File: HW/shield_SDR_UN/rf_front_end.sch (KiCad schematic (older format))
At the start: 93 parts, among them Q1 MOSFET_P, U1 MAX5864, U2 MAX2830

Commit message: Schematic finished
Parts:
- removed C?: 0, symbol Device:C
- removed FB?: FILTER, symbol hackrf-one-packages:FILTER
- removed P?: GSG-RF-CONN, symbol hackrf-one-rescue:GSG-RF-CONN
- removed R7, R? (x2): 4.7k, Resistor_SMD:R_0603_1608Metric_Pad1.05x0.95mm_HandSolder, symbol Device:R
- removed R? (x3): 0, symbol Device:R
- removed T?: BALUN, symbol hackrf-one-rescue:BALUN
- added C39: 0, Capacitor_SMD:C_0603_1608Metric_Pad1.05x0.95mm_HandSolder, symbol Device:C
- added P2: GSG-RF-CONN, lib:TAOGLAS_EMPCB.SMAFSTJ.B.HT, symbol hackrf-one-rescue:GSG-RF-CONN
- added R10, R11, R9: 0, Resistor_SMD:R_0603_1608Metric_Pad1.05x0.95mm_HandSolder, symbol Device:R
- added R13, R14, R15: 4.7k, Resistor_SMD:R_0603_1608Metric_Pad1.05x0.95mm_HandSolder, symbol Device:R
- added T1: BALUN, lib:HHM1711E1, symbol hackrf-one-rescue:BALUN
- C40: renamed from C?; footprint (none) -> Capacitor_SMD:C_0603_1608Metric_Pad1.05x0.95mm_HandSolder; Digikey RMCF0402ZT0R00CT-ND -> RMCF0603ZT0R00CT-ND
- FB1: footprint (none) -> Inductor_SMD:L_0805_2012Metric_Pad1.15x1.40mm_HandSolder; Digikey (none) -> BLM21PG221SN1D
- P1: renamed from P?; footprint (none) -> lib:TAOGLAS_EMPCB.SMAFSTJ.B.HT; Digikey (none) -> CON-SMA-EDGE-S-ND
- Q1: footprint (none) -> DMP2305U-7:SOT103P240X110-3N; Digikey (none) -> DMP2305UDICT-ND
- R12: renamed from R?; footprint (none) -> Resistor_SMD:R_0603_1608Metric_Pad1.05x0.95mm_HandSolder; Digikey RMCF0402ZT0R00CT-ND -> RMCF0603ZT0R00CT-ND
- R16: renamed from R?; DESCRIPTION 4.7 kOhms ±1% 0.1W, 1/10W -> (none); DIGIKEY 311-4.70KHRCT-ND -> (none); Digikey (none) -> 311-4.70KHRCT-ND
- T2: renamed from T?; footprint (none) -> lib:HHM1711E1; Digikey (none) -> 445-172632-1-ND
- gave numbers to parts that had none: 69
- renumbered C5 to C10, C2 to C5, C3 to C6, R6 to R20, U2 to U1, U1 to U3
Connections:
- net GNDA is gone; now on net GND: C11.2, C12.2, C13.2, C14.2, C15.2, C16.2, C17.2, C18.2, C19.2, C2.2, C20.2, C21.2, C22.2, C23.2, C24.2, C25.2, C26.2, C27.2, C28.2, C29.2, C3.2, C30.2, C31.2, C32.2, C33.2, C34.2, C35.2, C36.2, C37.2, C38.2, C4.2, C41.2, C42.2, C44.1, C45.1, C47.1, C48.1, C5.2, C7.2, C8.2, C9.2, CA1.2, D1.1 (K), P1.2 (GND), R16.1, T2.2 (S2), T2.5 (PM), U1.0 (EP), U1.2 (GNDRXLNA), U1.26 (GNDCP), U1.31 (GNDVCO), U3.0 (EP), U3.12 (GND), U3.37 (GND), U3.42 (GND), U3.5 (GND), U3.7 (GND)
- net GND: now also P2.2 (GND), R13.1, R14.1, R15.1, T1.2 (S2), T1.5 (PM)
- net IA+: now also R9.2
- net IA-: now also R10.2
- net QA-: now also R11.2
- net RXBBI+: now also R9.1
- net RXBBI-: now also R10.1
- net RXBBQ+: now also R11.1
- net TXBBI+: now also R13.2
- net TXBBI-: now also R14.2
- net TXBBQ+: now also R15.2
- net at U1.4 (ANT1+): now also T1.4 (PR2)
- net at U1.5 (ANT1-): now also T1.3 (PR1)
- net at U1.9 (ANT2+): now also C39.1
- net at P1.1 (RF): now also T1.1 (S1)
- net at T2.1 (S1): now also P2.1 (RF)
- net at T2.4 (PR2): now also C39.2
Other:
- note removed: "OJO CON ESTOS PINES LOS COLOQUE \nCOMO EL HACK COMUNICACION CON EL MICRO"

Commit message: organizacion PCB
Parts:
- Q1: footprint DMP2305U-7:SOT103P240X110-3N -> lib:SOT103P240X110-3N
- U1: footprint FP-MAX2830:MAX2830ETM&plus_ -> lib:MAX2830ETM&plus_
- U2: footprint QFN50P300X300X60-21N:QFN50P300X300X60-21N -> lib:QFN50P300X300X60-21N
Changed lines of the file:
@@
 Text Label 11800 3650 0    50   ~ 0
 REFP
-Text Label 14350 4050 0    50   ~ 0
+Text Label 14600 4050 2    50   ~ 0
 adDD9
-Text Label 14350 4150 0    50   ~ 0
+Text Label 14600 4150 2    50   ~ 0
 adDD8
-Text Label 14350 4250 0    50   ~ 0
+Text Label 14600 4250 2    50   ~ 0
 adDD7
-Text Label 14350 4350 0    50   ~ 0
+Text Label 14600 4350 2    50   ~ 0
 adDD6
-Text Label 14350 4450 0    50   ~ 0
+Text Label 14600 4450 2    50   ~ 0
 adDD5
-Text Label 14350 4550 0    50   ~ 0
+Text Label 14600 4550 2    50   ~ 0
 adDD4
-Text Label 14350 4650 0    50   ~ 0
+Text Label 14600 4650 2    50   ~ 0
 adDD3
-Text Label 14350 4750 0    50   ~ 0
+Text Label 14600 4750 2    50   ~ 0
 adDD2
 Text Label 13700 5650 1    50   ~ 0
@@
 QA+
 Wire Wire Line
-	13600 5400 13600 5800
-Wire Wire Line
 	13700 5400 13700 5800
-Wire Wire Line
-	14350 4050 14700 4050
-Wire Wire Line
-	14350 4150 14700 4150
-Wire Wire Line
-	14350 4250 14700 4250
-Wire Wire Line
-	14350 4350 14700 4350
-Wire Wire Line
-	14350 4450 14700 4450
-Wire Wire Line
-	14350 4550 14700 4550
-Wire Wire Line
-	14350 4650 14700 4650
-Wire Wire Line
-	14350 4750 14700 4750
-Text GLabel 14700 4050 2    50   Input ~ 0
+Text GLabel 14800 4050 2    50   Input ~ 0
 adDD9
-Text GLabel 14700 4150 2    50   Input ~ 0
+Text GLabel 14800 4150 2    50   Input ~ 0
 adDD8
-Text GLabel 14700 4250 2    50   Input ~ 0
+Text GLabel 14800 4250 2    50   Input ~ 0
 adDD7
-Text GLabel 14700 4350 2    50   Input ~ 0
+Text GLabel 14800 4350 2    50   Input ~ 0
 adDD6
-Text GLabel 14700 4450 2    50   Input ~ 0
+Text GLabel 14800 4450 2    50   Input ~ 0
 adDD5
-Text GLabel 14700 4550 2    50   Input ~ 0
+Text GLabel 14800 4550 2    50   Input ~ 0
 adDD4
-Text GLabel 14700 4650 2    50   Input ~ 0
+Text GLabel 14800 4650 2    50   Input ~ 0
 adDD3
-Text GLabel 14700 4750 2    50   Input ~ 0
+Text GLabel 14800 4750 2    50   Input ~ 0
 adDD2
 Text GLabel 13700 5800 3    50   Input ~ 0
@@
 adDA0
 Wire Wire Line
-	12800 2900 12800 3000
-Wire Wire Line
 	13100 2900 13100 3000
 Wire Wire Line
@@
 L power:VAA #PWR069
 U 1 1 5CCBDAAC
-P 14500 3950
-F 0 "#PWR069" H 14500 3800 50  0001 C CNN
-F 1 "VAA" V 14500 4150 50  0000 C CNN
-F 2 "" H 14500 3950 50  0001 C CNN
-F 3 "" H 14500 3950 50  0001 C CNN
-	1    14500 3950
+P 14550 3950
+F 0 "#PWR069" H 14550 3800 50  0001 C CNN
+F 1 "VAA" V 14550 4150 50  0000 C CNN
+F 2 "" H 14550 3950 50  0001 C CNN
+F 3 "" H 14550 3950 50  0001 C CNN
+	1    14550 3950
 	0    1    1    0
 $EndComp
-Wire Wire Line
-	14500 3950 14350 3950
 $Comp
 L power:VAA #PWR057
@@
 F 0 "Q1" H 1150 1250 60  0000 L CNN
 F 1 "MOSFET_P" H 800 1550 60  0000 L CNN
-F 2 "DMP2305U-7:SOT103P240X110-3N" H 1350 1400 60  0001 C CNN
+F 2 "lib:SOT103P240X110-3N" H 1350 1400 60  0001 C CNN
 F 3 "https://www.diodes.com/assets/Datasheets/ds31737.pdf" H 1350 1400 60  0001 C CNN
 F 4 "DMP2305UDICT-ND" H 1350 1400 50  0001 C CNN "Digikey"
@@
 	1250 3200 1250 3100
 $Comp
-L power:VCC #PWR064
-U 1 1 5CD923B4
-P 13100 5500
-F 0 "#PWR064" H 13100 5350 50  0001 C CNN
-F 1 "VCC" V 13100 5700 50  0000 C CNN
-F 2 "" H 13100 5500 50  0001 C CNN
-F 3 "" H 13100 5500 50  0001 C CNN
-	1    13100 5500
-	-1   0    0    1
-$EndComp
-Wire Wire Line
-	13100 5500 13100 5400
-$Comp
 L Device:C C5
 U 1 1 5CD06356
@@
 L power:VAA #PWR02
 U 1 1 5CDED280
-P 1200 7450
-F 0 "#PWR02" H 1200 7300 50  0001 C CNN
-F 1 "VAA" H 1200 7600 50  0000 C CNN
-F 2 "" H 1200 7450 50  0001 C CNN
-F 3 "" H 1200 7450 50  0001 C CNN
-	1    1200 7450
+P 1200 7400
+F 0 "#PWR02" H 1200 7250 50  0001 C CNN
+F 1 "VAA" H 1200 7550 50  0000 C CNN
+F 2 "" H 1200 7400 50  0001 C CNN
+F 3 "" H 1200 7400 50  0001 C CNN
+	1    1200 7400
 	1    0    0    -1
 $EndComp
@@
 	1200 8200 1200 8150
 Wire Wire Line
-	1200 7450 1200 7550
-Wire Wire Line
 	1600 7700 1600 7550
 Wire Wire Line
 	1600 7550 1200 7550
-Connection ~ 1200 7550
 Wire Wire Line
 	1200 7550 1200 7700
@@
 F 0 "U1" H 7600 4350 60  0000 L CNN
 F 1 "MAX2830" H 7450 4250 60  0000 L CNN
-F 2 "FP-MAX2830:MAX2830ETM&plus_" H 7650 4300 60  0001 C CNN
+F 2 "lib:MAX2830ETM&plus_" H 7650 4300 60  0001 C CNN
 F 3 "https://datasheets.maximintegrated.com/en/ds/MAX2830.pdf" H 7650 4300 60  0001 C CNN
 F 4 "MAX2830ETM+TCT-ND" H 7650 4300 50  0001 C CNN "Digikey"
@@
 	9000 4750 8850 4750
 $Comp
-L power:VAA #PWR025
-U 1 1 5CDC13A5
-P 6300 3750
-F 0 "#PWR025" H 6300 3600 50  0001 C CNN
-F 1 "VAA" V 6300 3950 50  0000 C CNN
-F 2 "" H 6300 3750 50  0001 C CNN
-F 3 "" H 6300 3750 50  0001 C CNN
-	1    6300 3750
-	0    -1   -1   0
-$EndComp
-$Comp
 L power:VAA #PWR027
 U 1 1 5CDC41DC
@@
 	9000 4350 8850 4350
 Wire Wire Line
-	9000 4650 8850 4650
-Wire Wire Line
 	8850 4850 9000 4850
 Wire Wire Line
@@
 NoConn ~ 10650 8950
 NoConn ~ 10550 8950
-Text GLabel 10850 9250 3    50   Input ~ 0
-3V3 MCU
-Wire Wire Line
-	10850 9250 10850 8950
 Wire Wire Line
 	11250 9100 10750 9100
@@
 Text GLabel 11800 9100 2    50   Input ~ 0
 GPIO_CLK
-Text GLabel 11800 8350 2    50   Input ~ 0
-3V3 MCU
-Wire Wire Line
-	11800 8350 11450 8350
-Text GLabel 10450 6800 1    50   Input ~ 0
-3V3 MCU
 $Comp
 L power:GND #PWR046
@@
 Text Notes 11550 7900 0    50   ~ 0
 MCU GP_CLKIN
-Text GLabel 11550 8050 2    50   Input ~ 0
-3V3 MCU
 Wire Wire Line
 	11550 8050 11450 8050
-Text GLabel 10650 7200 1    50   Input ~ 0
-3V3 MCU
-Wire Wire Line
-	10650 7200 10650 7350
 NoConn ~ 10550 7350
 $Comp
@@
 	1    0    0    -1
 $EndComp
-Text GLabel 8850 7550 1    50   Input ~ 0
-3V3 MCU
-Text GLabel 8650 7550 1    50   Input ~ 0
-3V3 MCU
-Text GLabel 8450 7550 1    50   Input ~ 0
-3V3 MCU
 Wire Wire Line
 	8450 7550 8450 7750
@@
 L power:VAA #PWR06
 U 1 1 5CEC6014
-P 1200 10100
-F 0 "#PWR06" H 1200 9950 50  0001 C CNN
-F 1 "VAA" H 1200 10250 50  0000 C CNN
-F 2 "" H 1200 10100 50  0001 C CNN
-F 3 "" H 1200 10100 50  0001 C CNN
-	1    1200 10100
+P 1200 10050
+F 0 "#PWR06" H 1200 9900 50  0001 C CNN
+F 1 "VAA" H 1200 10200 50  0000 C CNN
+F 2 "" H 1200 10050 50  0001 C CNN
+F 3 "" H 1200 10050 50  0001 C CNN
+	1    1200 10050
 	1    0    0    -1
 $EndComp
@@
 	1200 10850 1200 10800
 Wire Wire Line
-	1200 10100 1200 10200
-Wire Wire Line
 	1600 10350 1600 10200
 Wire Wire Line
 	1600 10200 1200 10200
-Connection ~ 1200 10200
 Wire Wire Line
 	1200 10200 1200 10350
@@
 NoConn ~ 8850 3950
 Wire Wire Line
-	7200 3100 7200 2900
-Wire Wire Line
 	7100 3100 7100 2900
 Text GLabel 7200 2900 1    50   Input ~ 0
@@
 F 0 "U2" H 10600 8200 60  0000 L CNN
 F 1 "SI5351C" H 10450 8050 60  0000 L CNN
-F 2 "QFN50P300X300X60-21N:QFN50P300X300X60-21N" H 10650 8150 60  0001 C CNN
+F 2 "lib:QFN50P300X300X60-21N" H 10650 8150 60  0001 C CNN
 F 3 "https://www.silabs.com/documents/public/data-sheets/Si5351-B.pdf" H 10650 8150 60  0001 C CNN
 F 4 "336-5160-1-ND" H 10650 8150 50  0001 C CNN "Digikey"
@@
 	1    0    0    -1
 $EndComp
-Text GLabel 14000 6600 0    50   Input ~ 0
-3V3 MCU
 Wire Wire Line
 	13400 6850 13400 6800
@@
 	14000 6800 14300 6800
 Wire Wire Line
-	14000 6800 14000 6600
-Wire Wire Line
 	13700 6850 13700 6800
 Connection ~ 13700 6800
@@
 SPI1_SCK
 Wire Wire Line
-	6450 3750 6300 3750
-Wire Wire Line
 	1250 6700 1250 6600
 Connection ~ 1250 6600
 Wire Wire Line
 	2150 5450 2150 5350
+Wire Wire Line
+	9000 4650 8850 4650
+Wire Wire Line
+	12800 2900 12800 3000
+Wire Wire Line
+	11800 8350 11450 8350
+Wire Wire Line
+	7200 2900 7200 3100
+Wire Wire Line
+	14350 4550 14800 4550
+Wire Wire Line
+	14350 4450 14800 4450
+Wire Wire Line
+	14550 3950 14350 3950
+Wire Wire Line
+	1200 7400 1200 7550
+Connection ~ 1200 7550
+$Comp
+L power:VAA #PWR0155
+U 1 1 5CEEB354
+P 6200 3750
+F 0 "#PWR0155" H 6200 3600 50  0001 C CNN
+F 1 "VAA" V 6200 3950 50  0000 C CNN
+F 2 "" H 6200 3750 50  0001 C CNN
+F 3 "" H 6200 3750 50  0001 C CNN
+	1    6200 3750
+	0    -1   -1   0
+$EndComp
+Wire Wire Line
+	6200 3750 6450 3750
+Wire Wire Line
+	1200 10050 1200 10200
+Connection ~ 1200 10200
+$Comp
+L power:VCC #PWR0156
+U 1 1 5CF2950C
+P 13100 5800
+F 0 "#PWR0156" H 13100 5650 50  0001 C CNN
+F 1 "VCC" V 13100 6000 50  0000 C CNN
+F 2 "" H 13100 5800 50  0001 C CNN
+F 3 "" H 13100 5800 50  0001 C CNN
+	1    13100 5800
+	-1   0    0    1
+$EndComp
+Wire Wire Line
+	13100 5400 13100 5800
+Wire Wire Line
+	13600 5400 13600 5800
+Wire Wire Line
+	14350 4650 14800 4650
+Wire Wire Line
+	14350 4350 14800 4350
+Wire Wire Line
+	14350 4250 14800 4250
+Wire Wire Line
+	14350 4150 14800 4150
+Wire Wire Line
+	14350 4050 14800 4050
+Wire Wire Line
+	14350 4750 14800 4750
+Wire Wire Line
+	10650 7350 10650 6800
+Wire Wire Line
+	14000 6800 14000 6600
+Wire Wire Line
+	14000 6600 13850 6600
+Text GLabel 10850 9350 3    50   Input ~ 0
+3V3 MCU
+Wire Wire Line
+	10850 8950 10850 9350
+Text GLabel 11800 8350 2    50   Input ~ 0
+3V3 MCU
+Text GLabel 11550 8050 2    50   Input ~ 0
+3V3 MCU
+Text GLabel 10450 6800 1    50   Input ~ 0
+3V3 MCU
+Text GLabel 10650 6800 1    50   Input ~ 0
+3V3 MCU
+Text GLabel 8450 7550 1    50   Input ~ 0
+3V3 MCU
+Text GLabel 8650 7550 1    50   Input ~ 0
+3V3 MCU
+Text GLabel 8850 7550 1    50   Input ~ 0
+3V3 MCU
+Text GLabel 13850 6600 0    50   Input ~ 0
+3V3 MCU
 $EndSCHEMATC

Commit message: Omega 2 PCB
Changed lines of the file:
@@
 Text Label 11800 3650 0    50   ~ 0
 REFP
-Text Label 14600 4050 2    50   ~ 0
+Text Label 14675 4050 2    50   ~ 0
 adDD9
 Text Label 14600 4150 2    50   ~ 0
@@
 $EndComp
 Wire Wire Line
-	7300 2950 7300 3100
-Wire Wire Line
 	7800 2950 7800 3100
 Wire Wire Line
@@
 	14350 4150 14800 4150
 Wire Wire Line
-	14350 4050 14800 4050
-Wire Wire Line
 	14350 4750 14800 4750
 Wire Wire Line
@@
 Text GLabel 13850 6600 0    50   Input ~ 0
 3V3 MCU
+Wire Wire Line
+	14350 4050 14800 4050
+Wire Wire Line
+	7300 2950 7300 3100
 $EndSCHEMATC

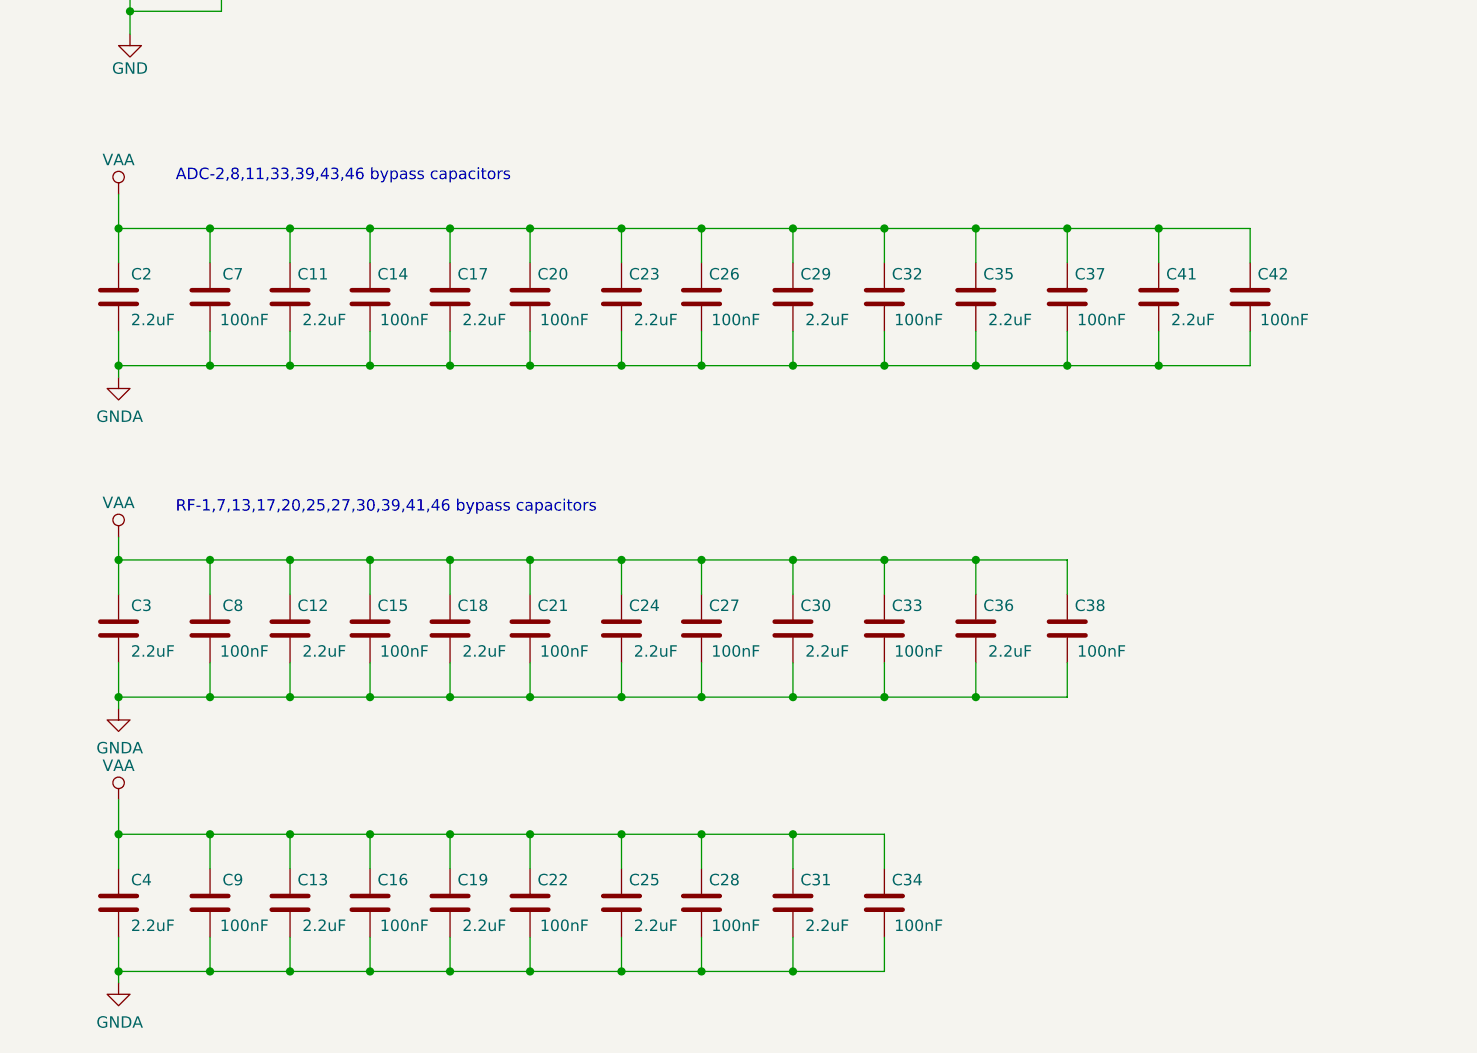
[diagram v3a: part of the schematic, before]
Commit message: Capacitors of RF front-end edited, components placed in the PCB
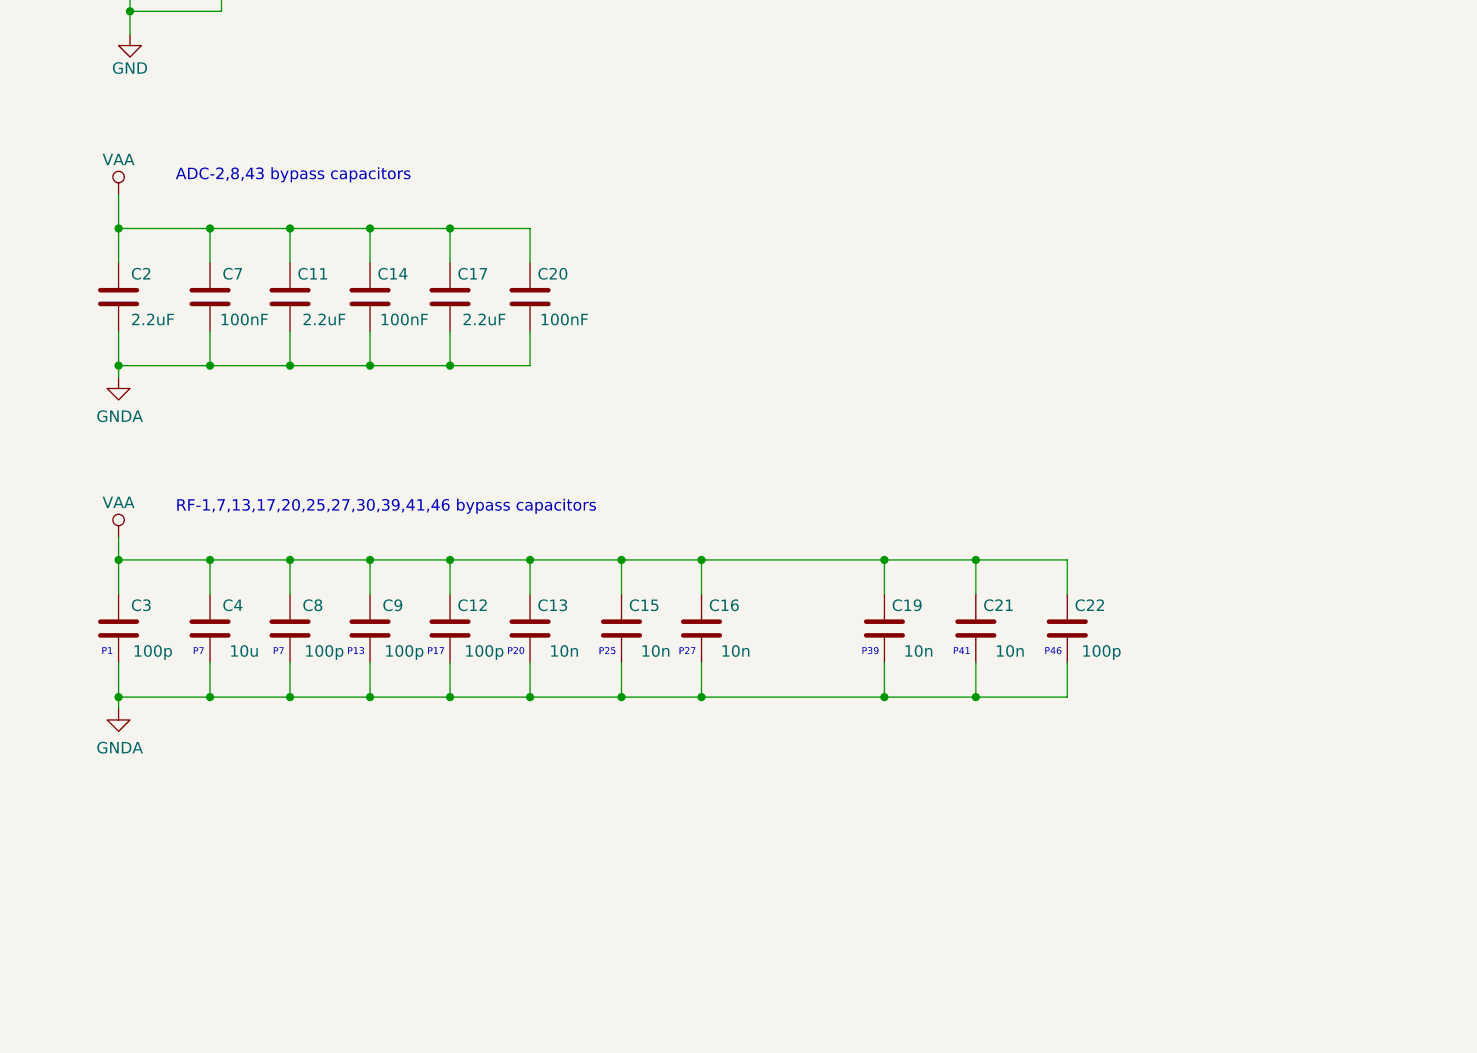
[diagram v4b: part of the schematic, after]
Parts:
- removed C18, C23, C24, C25, C29, C30, C31, C35, C36, C41: 2.2uF, Capacitor_SMD:C_0603_1608Metric_Pad1.05x0.95mm_HandSolder, symbol Device:C
- removed C26, C27, C28, C32, C33, C34, C37, C38, C42: 100nF, Capacitor_SMD:C_0603_1608Metric_Pad1.05x0.95mm_HandSolder, symbol Device:C
- C12, C3: value 2.2uF -> 100p; Digikey 1276-1183-1-ND -> 1276-1909-1-ND
- C13, C19: value 2.2uF -> 10n; Digikey 1276-1183-1-ND -> 1276-1009-1-ND
- C15, C16, C21: value 100nF -> 10n; Digikey 1276-1000-1-ND -> 1276-1009-1-ND
- C22, C8, C9: value 100nF -> 100p; Digikey 1276-1000-1-ND -> 1276-1909-1-ND
- C39, C40: footprint Capacitor_SMD:C_0603_1608Metric_Pad1.05x0.95mm_HandSolder -> Capacitor_SMD:C_0402_1005Metric; Digikey RMCF0603ZT0R00CT-ND -> 311-0.0JRCT-ND
- C4: value 2.2uF -> 10u; Digikey 1276-1183-1-ND -> 1276-1192-1-ND
- C5: footprint Capacitor_SMD:C_0805_2012Metric_Pad1.15x1.40mm_HandSolder -> Capacitor_SMD:C_0603_1608Metric_Pad1.05x0.95mm_HandSolder
- R22, R23: Digikey (none) -> 311-39.0HRCT-ND; digikey 311-39.0HRCT-ND -> (none)
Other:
- note added: "ADC-2,8,43 bypass capacitors"
- note added: "P1"
- note added: "P13"
- note added: "P17"
- note added: "P20"
- note added: "P25"
- note added: "P27"
- note added: "P39"
- note added: "P41"
- note added: "P46"
- note added: "P7"
- note removed: "ADC-2,8,11,33,39,43,46 bypass capacitors"

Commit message: PCB route V4
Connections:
- net I2C_SCL: now also R5.2, U2.4 (SCL); no longer R4.2, U2.5 (SDA)
- net I2C_SDA: now also R4.2, U2.5 (SDA); no longer R5.2, U2.4 (SCL)
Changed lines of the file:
@@
 Text Label 4850 2200 2    50   ~ 0
 I2C1_SCL
-Text GLabel 4450 2300 0    50   Input ~ 0
+Text GLabel 7900 8250 0    50   Input ~ 0
 I2C_SCL
-Text GLabel 4450 2200 0    50   Input ~ 0
+Text GLabel 7900 8350 0    50   Input ~ 0
 I2C_SDA
 Wire Wire Line
@@
 Wire Wire Line
 	3750 9000 4550 9000
+Text GLabel 7300 5950 3    50   BiDi ~ 0
+SPI1_CS_RF
+Text GLabel 7800 6850 3    50   BiDi ~ 0
+SPI1_MISO
+Text GLabel 14750 3650 2    50   BiDi ~ 0
+SPI1_CS_AD
+Text GLabel 7700 6850 3    50   BiDi ~ 0
+SPI1_MOSI
+Text GLabel 7600 5950 3    50   BiDi ~ 0
+SPI1_SCK
+Text GLabel 14750 3850 2    50   BiDi ~ 0
+SPI1_MISO
+Text GLabel 14750 3750 2    50   BiDi ~ 0
+SPI1_SCK
+Text GLabel 4450 2200 0    50   Input ~ 0
+I2C_SCL
+Text GLabel 4450 2300 0    50   Input ~ 0
+I2C_SDA
 $EndSCHEMATC
